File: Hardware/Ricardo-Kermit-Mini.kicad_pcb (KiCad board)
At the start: 4 copper layers, 84 x 43 mm, 209 parts, among them IC1 TPS61089RNRR, IC2 AP2205-W5-7, IC3 AP2205-W5-7, IC4 TPS61089RNRR, IC5 ADS131M04IRUKR, J1 RBUS, J2 USB_C_Receptacle_USB2.0, J3 Micro_SD_Card_Det, J4 1053131104, J5 1053131104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

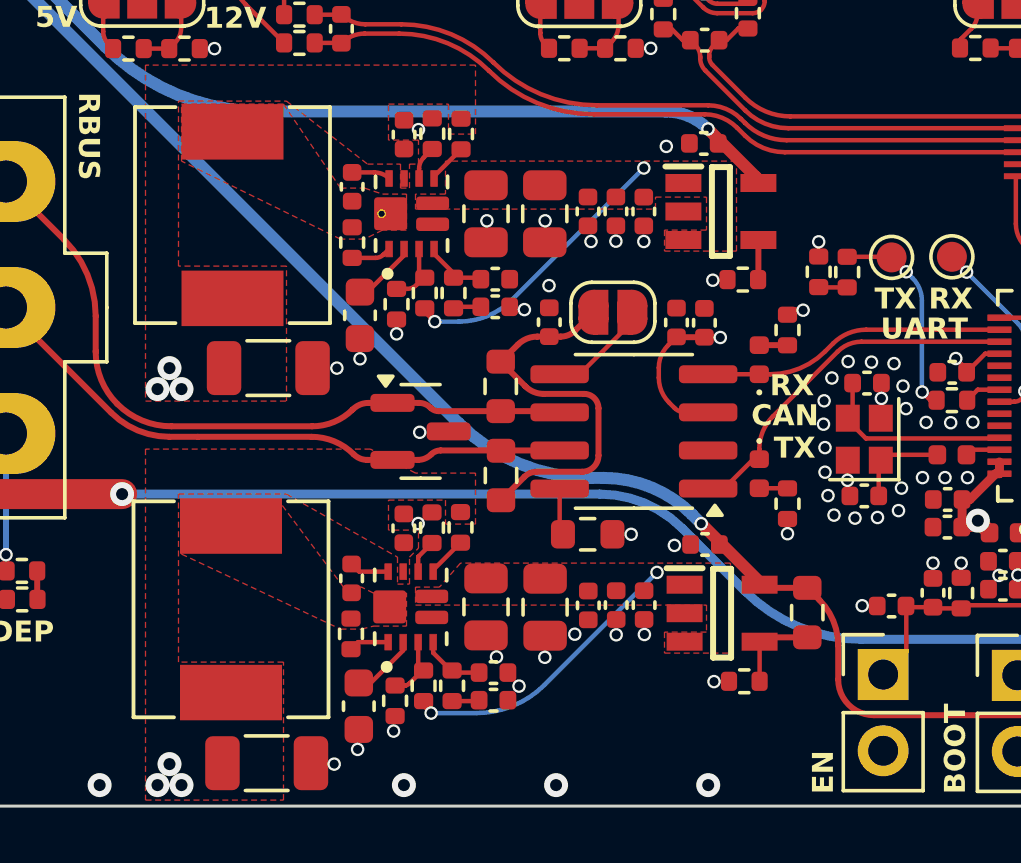
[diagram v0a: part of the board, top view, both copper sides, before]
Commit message: changed ldo output to 12v, kiran review done
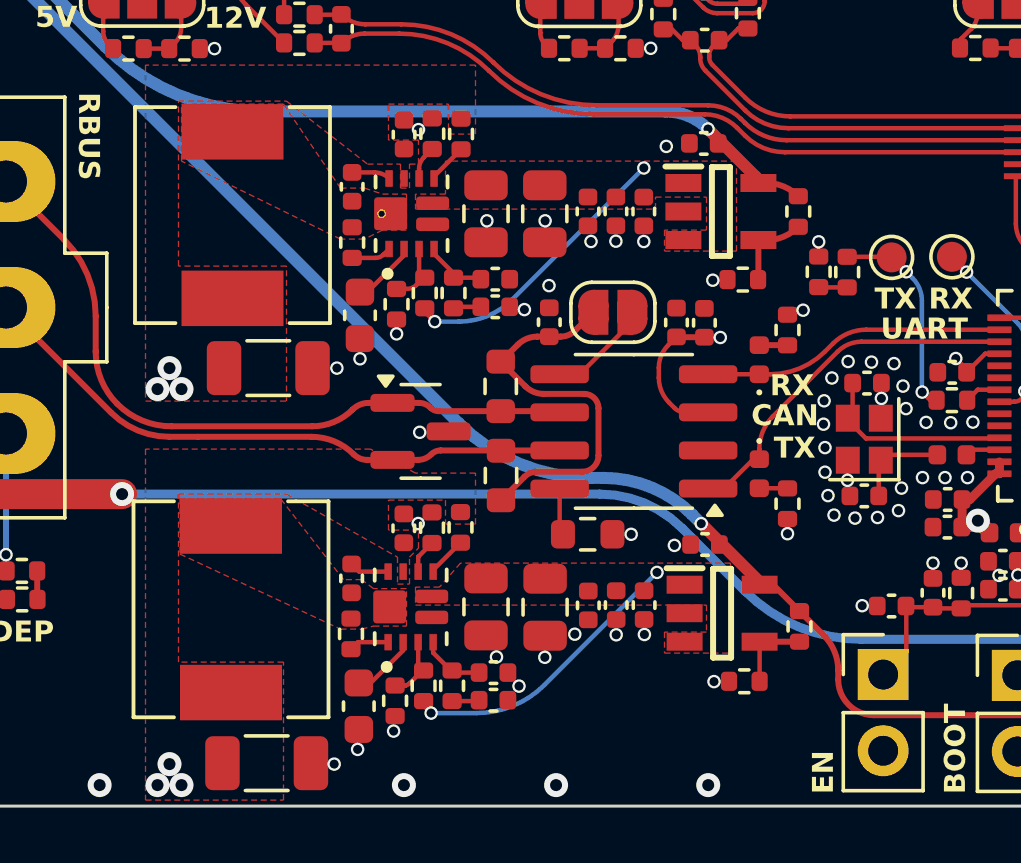
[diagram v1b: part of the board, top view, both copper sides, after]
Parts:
- added R65: 360k, Resistor_SMD:R_0402_1005Metric, F.Cu at (21.8, 37.8)
- R23: footprint Resistor_SMD:R_0603_1608Metric -> Resistor_SMD:R_0402_1005Metric
- R26: value 900k -> 976k
- moved R23 0.53 mm to (21.8, 51.6)
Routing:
- net Net-(IC3-ADJ/NC): track 1.32 -> 2.77 mm
- net +12V: track 80.4 -> 81.8 mm
- net +5V: track 107.5 -> 106.9 mm

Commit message: hope shiven is happy
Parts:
- moved J1 31.1 mm to (19.5, 54.8), turned to 180 degrees
- moved R22 29.0 mm to (-8.43, 47.5), turned to -90 degrees
- moved C34 28.9 mm to (-11.2, 31.5), turned to -90 degrees
- moved R23 28.5 mm to (-6.59, 49.3), turned to 0 degrees
- moved 12VLED1 27.7 mm to (23.6, 49.9)
- moved R7 27.7 mm to (23.6, 49.0)
- moved IC2 25.8 mm to (-6.16, 46.7), turned to -90 degrees
- moved C12 25.6 mm to (-9.26, 34.6), turned to 180 degrees
- moved C19 25.5 mm to (-9.05, 39.1), turned to -90 degrees
- moved R19 25.2 mm to (-9.07, 35.8), turned to 0 degrees
- moved R5 24.6 mm to (-8.57, 37.7), turned to 180 degrees
- moved R18 24.5 mm to (-8.58, 36.8), turned to 180 degrees
- moved C18 24.2 mm to (-8.13, 39.1), turned to -90 degrees
- moved C36 23.5 mm to (-5.88, 44.1), turned to 180 degrees
- moved C32 23.4 mm to (-4.75, 49.3), turned to 0 degrees
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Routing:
- net RBUS_uC_V: track 67.2 -> 37.8 mm, vias 2 -> 1
- net +5V: track 106.9 -> 127.5 mm
- net +12V: track 81.8 -> 61.8 mm
- net /CAN-: track 23.9 -> 13.3 mm
- net /CAN+: track 20.4 -> 11.5 mm
- net /CAN_TX: track 12.8 -> 7.98 mm
- net /pressure_sensor1/AIN2P: track 13.6 -> 10.3 mm
- net /pressure_sensor1/AIN2N: track 13.3 -> 10.5 mm
- net /pressure_sensor1/AIN3P: track 24.5 -> 21.9 mm
- net /pressure_sensor1/AIN3N: track 24.4 -> 21.9 mm
- net /pressure_sensor1/AIN0N: track 17.6 -> 15.3 mm
- net /pressure_sensor1/AIN0P: track 18.0 -> 15.7 mm
- net /Boosts/LDO5.5V_IN: track 9.82 -> 8.23 mm
- net /CAN_RX: track 10.1 -> 8.65 mm
- net Net-(JP21-B): track 7.24 -> 8.64 mm
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
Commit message: update
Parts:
- R23: value 152k -> 150k
